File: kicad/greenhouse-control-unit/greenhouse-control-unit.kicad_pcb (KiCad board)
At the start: 2 copper layers, 252.1 x 133.3 mm, 43 parts, among them J1 Screw_Terminal_01x02, J10_Buck2 Conn_01x01_Female, J11_Buck2 Conn_01x01_Female, J12_Buck1 Conn_01x01_Female, J13_Buck1 Conn_01x01_Female, J14_Buck2 Conn_01x01_Female, J15_Buck2 Conn_01x01_Female, J16 Screw_Terminal_01x16, J2 Screw_Terminal_01x02, J3 Screw_Terminal_01x02, J4 Screw_Terminal_01x06, J5 Conn_01x03_Male, J6 Conn_01x02_Male, J6_BigBuck1 Conn_01x01_Female, J7_Buck1 Conn_01x01_Female, J8 Conn_01x15_Female, J9 Conn_01x15_Female, Q1 IRLB8721PBF, Q2 IRLB8721PBF, Q3 IRLB8721PBF, Q4 IRLB8721PBF, Q6 2N2222A, Q7 2N2222A, Q8 2N2222A, Q9 IRLB8721PBF, U1 74HC595, U2 74HC595

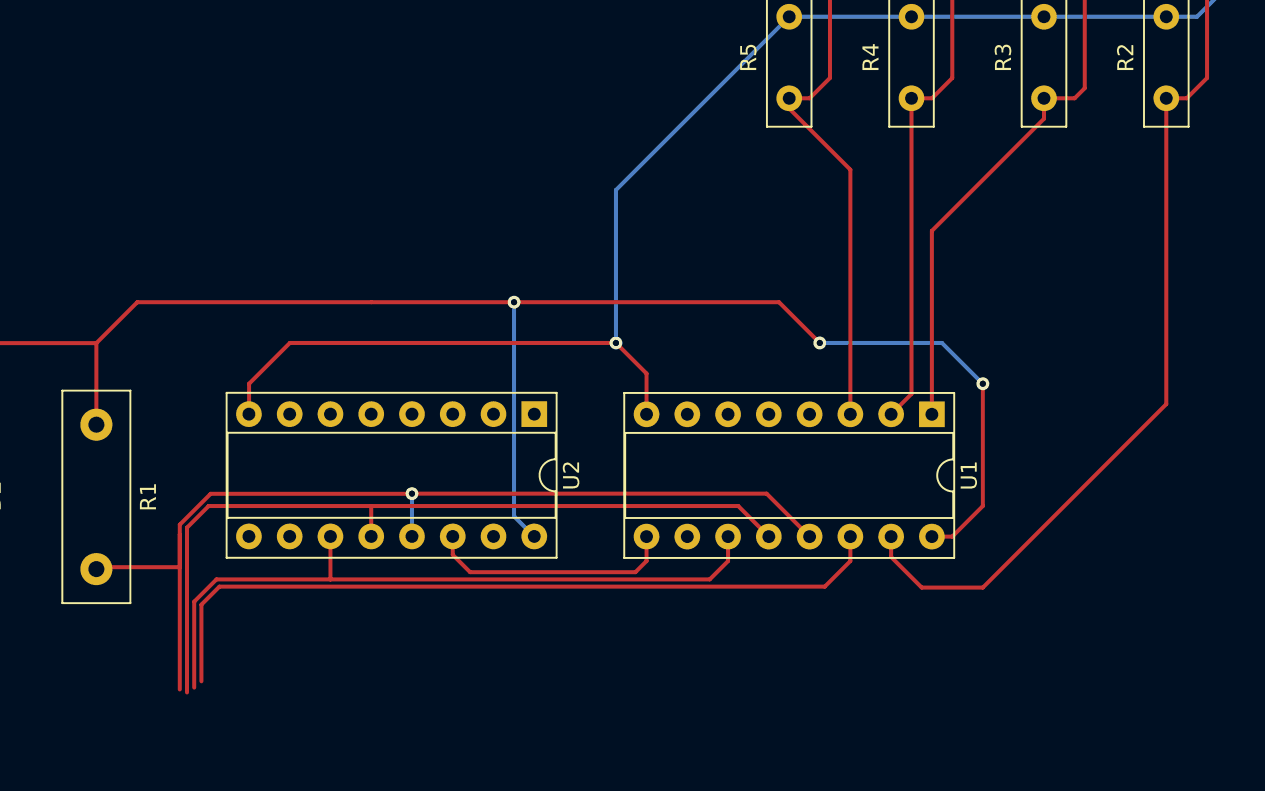
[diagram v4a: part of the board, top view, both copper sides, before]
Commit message: Swap U1 and U2 positions on PCB
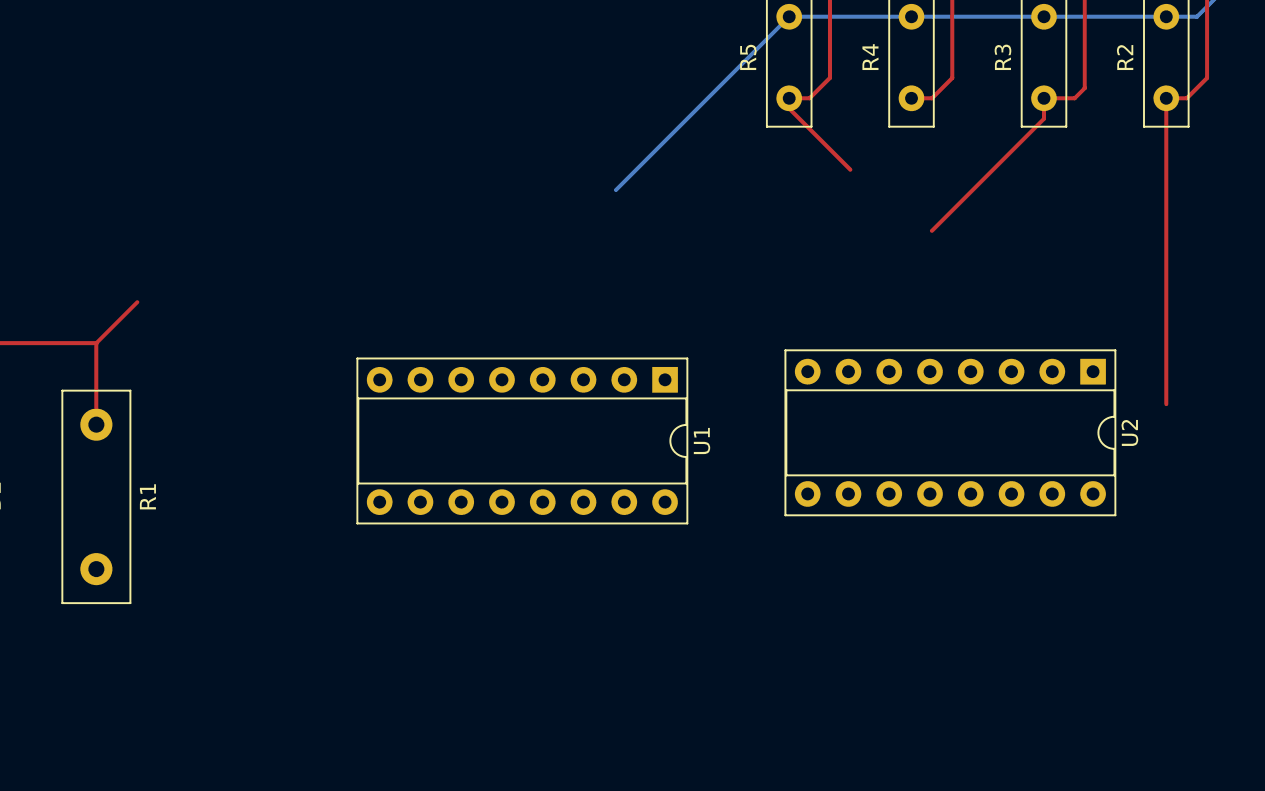
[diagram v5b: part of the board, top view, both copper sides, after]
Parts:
- moved U2 34.9 mm to (187.2, 80.5)
- moved U1 16.8 mm to (160.5, 81.0)
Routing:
- net /SR_VCC: track 102.4 -> 20.9 mm, vias 3 -> 0
- net /MC_D8: track 61.4 -> 0.17 mm, vias 1 -> 0
- net /MC_D5: track 106.3 -> 56.5 mm
- net /MC_D6: track 105.8 -> 57.9 mm
- net /MC_D7: track 103.2 -> 59.3 mm
- net GND: track 353.1 -> 311.9 mm, vias 4 -> 3
- net /SW1_SR_Q08: track 58.1 -> 34.1 mm
- net /SW3_SR_Q10: track 35.3 -> 15.1 mm
- net Net-(U1-Pad9): track 15.5 -> 0.00 mm
- net /SW4_SR_Q11: track 36.3 -> 21.1 mm
- net /SW2_SR_Q09: track 38.0 -> 26.6 mm

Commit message: Rearranged PCB layout, re-annotate power connectors
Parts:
- removed the D4 at (203.8, 112.4)
- removed D5: 1N4001, Diode_THT:D_DO-41_SOD81_P10.16mm_Horizontal
- added J6: Screw_Terminal_01x02, TerminalBlock_Phoenix:TerminalBlock_Phoenix_MKDS-1,5-2-5.08_1x02_P5.08mm_Horizontal, F.Cu at (186.5, 34.0)
- added J7: Screw_Terminal_01x02, TerminalBlock_Phoenix:TerminalBlock_Phoenix_MKDS-1,5-2-5.08_1x02_P5.08mm_Horizontal, F.Cu at (171.0, 34.0)
- added J8: Conn_01x03_Male, Connector_Molex:Molex_KK-254_AE-6410-03A_1x03_P2.54mm_Vertical, F.Cu at (259.0, 50.0)
- J4: value Screw_Terminal_01x06 -> Screw_Terminal_01x02; footprint TerminalBlock_Phoenix:TerminalBlock_Phoenix_MKDS-1,5-6-5.08_1x06_P5.08mm_Horizontal -> TerminalBlock_Phoenix:TerminalBlock_Phoenix_MKDS-1,5-2-5.08_1x02_P5.08mm_Horizontal
- J5: value Conn_01x03_Male -> Screw_Terminal_01x02; footprint Connector_Molex:Molex_KK-254_AE-6410-03A_1x03_P2.54mm_Vertical -> TerminalBlock_Phoenix:TerminalBlock_Phoenix_MKDS-1,5-2-5.08_1x02_P5.08mm_Horizontal
- moved J5 111.7 mm to (202.0, 34.0), turned to 180 degrees
- moved J4 91.3 mm to (217.5, 34.0), turned to 180 degrees
- moved Q3 89.2 mm to (192.7, 63.4)
- moved Q2 68.5 mm to (263.0, 62.0), turned to 180 degrees
- moved J3 47.6 mm to (233.0, 34.0), turned to 180 degrees
- moved J12 43.1 mm to (152.6, 34.1)
- moved Q5 43.1 mm to (125.6, 53.7)
- moved Q6 43.1 mm to (149.1, 53.7)
- moved Q7 43.1 mm to (141.4, 53.7)
- moved Q8 43.1 mm to (133.2, 53.7)
- moved R6 43.1 mm to (125.3, 65.2)
- moved R7 43.1 mm to (148.8, 65.2)
- moved R8 43.1 mm to (141.1, 65.2)
- moved R9 43.1 mm to (132.9, 65.2)
- moved BZ1 37.7 mm to (190.2, 144.0)
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- renumbered D2 to D1, D6 to D2, D1 to D4, J9 to J10, J10_Buck2 to J10_LittleBuck1, J6 to J11, J11_Buck2 to J11_LittleBuck1, J16 to J12, J12_Buck1 to J12_BigBuck1, J13_Buck1 to J13_BigBuck1, J14_Buck2 to J14_LittleBuck1, J15_Buck2 to J15_LittleBuck1, J7_Buck1 to J7_BigBuck1, J8 to J9, Q9 to Q1, Q8 to Q2, Q6 to Q3, Q7 to Q4, Q4 to Q5, Q1 to Q6, Q2 to Q7, Q3 to Q8, R6 to R2, R9 to R3, R8 to R4, R7 to R5, R5 to R6, R2 to R7, R3 to R8, R4 to R9
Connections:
- J1 pad 2: +12V -> /BattRelayNC_B
- J3 pad 1: GND -> /Batt+12V
- J3 pad 2: +12V -> /BattRelayNC_B
- J5 pad 1: +12V -> GND
- J5 pad 2: GND -> /BattRelayNC_B
- Q1 pad 2: /BattRelayNC_Coil -> /BattRelayNC_Boil
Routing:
- net +12V: track 490.2 -> 80.4 mm, vias 2 -> 0
- net /SR_VCC: track 20.9 -> 102.4 mm, vias 0 -> 3
- net /Batt+12V: track 69.8 -> 0.00 mm
- net /MC_D8: track 0.17 -> 61.4 mm, vias 0 -> 1
- net /MC_D5: track 56.5 -> 106.3 mm
- net /MC_D6: track 57.9 -> 105.8 mm
- net GND: track 311.9 -> 266.6 mm, vias 3 -> 2
- net /MC_D7: track 59.3 -> 103.2 mm
- net /BattRelayNC_SR_Q0: track 0.00 -> 23.9 mm
- net /SW1_SR_Q08: track 34.1 -> 15.1 mm
- net Net-(U1-Pad9): track 0.00 -> 15.5 mm
- net /SW2_SR_Q09: track 26.6 -> 16.7 mm
- net /SW4_SR_Q11: track 21.1 -> 15.7 mm
- net /CaseFan_SR_Q2: track 0.00 -> 1.80 mm
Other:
- board outline removed

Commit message: Add PSU diode, reorganize PCB layout
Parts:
- removed the J6 at (186.5, 34.0)
- added D1: D_Schottky, Package_TO_SOT_THT:TO-126-2_Vertical, F.Cu at (160.5, 34.4)
- added D2: LED, LED_THT:LED_D5.0mm, F.Cu at (162.0, 47.2)
- added D7: LED, LED_THT:LED_D5.0mm, F.Cu at (176.0, 47.0)
- added J13: Conn_01x10_Female, Connector_Molex:Molex_KK-254_AE-6410-10A_1x10_P2.54mm_Vertical, F.Cu at (47.0, 34.0)
- added J8: Conn_01x10_Female, Connector_PinSocket_2.54mm:PinSocket_1x10_P2.54mm_Vertical, F.Cu at (96.5, 97.0)
- added R1: 5k, Resistor_THT:R_Axial_DIN0207_L6.3mm_D2.5mm_P7.62mm_Horizontal, F.Cu at (176.0, 65.2)
- added R16: R10k, Resistor_THT:R_Axial_DIN0207_L6.3mm_D2.5mm_P7.62mm_Horizontal, F.Cu at (133.7, 57.2)
- added R2: 10k, Resistor_THT:R_Axial_DIN0207_L6.3mm_D2.5mm_P7.62mm_Horizontal, F.Cu at (183.0, 72.8)
- added R3: 5k, Resistor_THT:R_Axial_DIN0207_L6.3mm_D2.5mm_P7.62mm_Horizontal, F.Cu at (162.0, 65.2)
- added R4: 10k, Resistor_THT:R_Axial_DIN0207_L6.3mm_D2.5mm_P7.62mm_Horizontal, F.Cu at (169.0, 72.8)
- added R5: 10k, Resistor_THT:R_Axial_DIN0207_L6.3mm_D2.5mm_P7.62mm_Horizontal, F.Cu at (162.0, 60.8)
- added R6: 10k, Resistor_THT:R_Axial_DIN0207_L6.3mm_D2.5mm_P7.62mm_Horizontal, F.Cu at (102.5, 87.0)
- J10, J9: footprint Connector_PinHeader_2.54mm:PinHeader_1x15_P2.54mm_Vertical -> Connector_PinSocket_2.54mm:PinSocket_1x15_P2.54mm_Vertical
- J12_BigBuck1, J13_BigBuck1, J6_BigBuck1, J7_BigBuck1: footprint Connector_PinHeader_2.54mm:PinHeader_1x01_P2.54mm_Vertical -> Connector_PinSocket_2.54mm:PinSocket_1x01_P2.54mm_Vertical
- J7: value Screw_Terminal_01x02 -> Conn_01x10_Female; footprint TerminalBlock_Phoenix:TerminalBlock_Phoenix_MKDS-1,5-2-5.08_1x02_P5.08mm_Horizontal -> Connector_PinSocket_2.54mm:PinSocket_1x10_P2.54mm_Vertical
- R10: renamed from R2; value 10k -> R4k6; footprint Resistor_THT:R_Box_L8.4mm_W2.5mm_P5.08mm -> Resistor_THT:R_Axial_DIN0207_L6.3mm_D2.5mm_P7.62mm_Horizontal
- R11: renamed from R3; value 10k -> 2k; footprint Resistor_THT:R_Box_L8.4mm_W2.5mm_P5.08mm -> Resistor_THT:R_Axial_DIN0207_L6.3mm_D2.5mm_P7.62mm_Horizontal
- R12: renamed from R6; value R10k -> 2k; footprint Resistor_THT:R_Box_L8.4mm_W2.5mm_P5.08mm -> Resistor_THT:R_Axial_DIN0207_L6.3mm_D2.5mm_P7.62mm_Horizontal
- R13: renamed from R7; footprint Resistor_THT:R_Box_L8.4mm_W2.5mm_P5.08mm -> Resistor_THT:R_Axial_DIN0207_L6.3mm_D2.5mm_P7.62mm_Horizontal
- R14: renamed from R8; footprint Resistor_THT:R_Box_L8.4mm_W2.5mm_P5.08mm -> Resistor_THT:R_Axial_DIN0207_L6.3mm_D2.5mm_P7.62mm_Horizontal
- R15: renamed from R9; footprint Resistor_THT:R_Box_L8.4mm_W2.5mm_P5.08mm -> Resistor_THT:R_Axial_DIN0207_L6.3mm_D2.5mm_P7.62mm_Horizontal
- R7: renamed from R1; footprint Resistor_THT:R_Box_L13.0mm_W4.0mm_P9.00mm -> Resistor_THT:R_Axial_DIN0207_L6.3mm_D2.5mm_P7.62mm_Horizontal
- R8: renamed from R4; value R10k -> 2k; footprint Resistor_THT:R_Box_L8.4mm_W2.5mm_P5.08mm -> Resistor_THT:R_Axial_DIN0207_L6.3mm_D2.5mm_P7.62mm_Horizontal
- R9: renamed from R5; value R4k6 -> R10k; footprint Resistor_THT:R_Box_L13.0mm_W4.0mm_P9.00mm -> Resistor_THT:R_Axial_DIN0207_L6.3mm_D2.5mm_P7.62mm_Horizontal
- moved Q4 162.0 mm to (79.2, 43.4)
- moved J11 161.5 mm to (79.2, 34.0)
- moved Q1 119.8 mm to (207.0, 48.0), turned to 180 degrees
- moved D5 118.0 mm to (230.2, 120.0)
- moved J7 112.3 mm to (78.0, 96.9)
- moved R10 110.1 mm to (239.2, 124.0)
- moved R8 105.0 mm to (218.0, 60.5), turned to 90 degrees
- moved R11 95.8 mm to (190.0, 60.8), turned to 90 degrees
- moved D4 95.1 mm to (218.0, 47.0), turned to -90 degrees
- moved D6 94.3 mm to (190.0, 47.0), turned to -90 degrees
- moved J1 85.5 mm to (178.5, 34.0)
- moved J9 81.9 mm to (35.0, 64.4), turned to 0 degrees
- moved J14_LittleBuck1 69.2 mm to (217.0, 86.8)
- moved J15_LittleBuck1 69.2 mm to (232.9, 86.8)
- moved J10_LittleBuck1 69.2 mm to (217.0, 78.5)
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- renumbered D1 to D3, D2 to D5, D3 to D6, J8 to J6
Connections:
- net /MC_D6 renamed /SR_SER
- net /MC_D7 renamed /SR_CLK
- D4 pad 1: Net-(D4-Pad1) -> GND
- D4 pad 2: Net-(BZ1-Pad1) -> Net-(D4-Pad2)
- D5 pad 1: GND -> Net-(D5-Pad1)
- D5 pad 2: Net-(D2-Pad2) -> Net-(BZ1-Pad1)
- J1 pad 1: GND -> /PSU+12V
- J1 pad 2: /BattRelayNC_B -> GND
- J10 pad 1: /MC_D8 -> +3V3
- J10 pad 12: /MC_D3 -> /OneWire
- J10 pad 13: /I2C_SDA -> /ADC1_SCA
- J10 pad 14: /I2C_SCL -> /ADC1_SCL
- J10 pad 15: unconnected-(J10-Pad15) -> /MC_D0
- J2 pad 1: GND -> /Batt+12V
- J2 pad 2: /Batt+12V -> GND
- J3 pad 1: /Batt+12V -> +12V
- J3 pad 2: /BattRelayNC_B -> /Batt+12V
- J4 pad 1: GND -> /BattRelayNC_Coil
- J4 pad 2: /BattRelayNC_Coil -> GND
- J5 pad 1: GND -> +12V
- J5 pad 2: /BattRelayNC_B -> GND
- J7 pad 1: GND -> +5VA
- J7 pad 2: +12V -> GND
- J9 pad 1: /MC_A0 -> +5VA
- J9 pad 14: GND -> unconnected-(J9-Pad14)
- J9 pad 15: +5VA -> /MC_A0
- J9 pad 2: unconnected-(J9-Pad2) -> GND
- Q1 pad 2: /BattRelayNC_Boil -> /BattRelayNC_Coil
- R10 pad 1: /BatteryLed_SR_Q4 -> Net-(D5-Pad1)
- R10 pad 2: Net-(D2-Pad2) -> GND
- R11 pad 1: /PsuLed_SR_Q5 -> /BatteryLed_SR_Q4
- R12 pad 1: /SW4_SR_Q11 -> /PsuLed_SR_Q5
- R12 pad 2: GND -> Net-(D7-Pad2)
- R13 pad 1: /SW1_SR_Q08 -> /SW4_SR_Q11
- R14 pad 1: /SW2_SR_Q09 -> /SW1_SR_Q08
- R15 pad 1: /SW3_SR_Q10 -> /SW2_SR_Q09
- R7 pad 2: /MC_D8 -> /MC_D0
- R8 pad 1: GND -> /BattRelayNC_SR_Q0
- R8 pad 2: /StartBeep_SR_Q1 -> Net-(D4-Pad2)
- R9 pad 1: Net-(D4-Pad1) -> GND
- R9 pad 2: GND -> /StartBeep_SR_Q1
- U1 pad 13: /MC_D8 -> /MC_D0
- U2 pad 13: /MC_D8 -> /MC_D0
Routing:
- net +12V: track 80.4 -> 179.8 mm, vias 0 -> 1
- net GND: track 266.6 -> 335.8 mm
- net /MC_D0: track 0.00 -> 61.4 mm, vias 0 -> 1
- net /MC_D8: track 61.4 -> 0.00 mm, vias 1 -> 0
- net unconnected-(J10-Pad5): track 60.8 -> 0.00 mm
- net /SR_CLK: track 103.2 -> 43.9 mm
- net /SR_SER: track 105.8 -> 47.9 mm
- net /MC_D5: track 106.3 -> 49.8 mm
- net /PSU+12V: track 0.00 -> 52.5 mm, vias 0 -> 1
- net /BattRelayNC_Coil: track 0.00 -> 26.6 mm
- net /SW3_SR_Q10: track 15.1 -> 0.00 mm
- net /Batt+12V: track 0.00 -> 8.78 mm
- net /PSU_VoltageSensor_A: track 0.00 -> 7.00 mm
- net /COM_VoltageSensor_A: track 0.00 -> 7.00 mm
- net Net-(D7-Pad2): track 0.00 -> 3.65 mm
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
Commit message: Connect relay coil to VCC, fixed footprints
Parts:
- J5: value Screw_Terminal_01x02 -> Conn_01x02_Male; footprint TerminalBlock_Phoenix:TerminalBlock_Phoenix_MKDS-1,5-2-5.08_1x02_P5.08mm_Horizontal -> Connector_Molex:Molex_KK-254_AE-6410-02A_1x02_P2.54mm_Vertical
- moved J5 139.5 mm to (94.5, 39.0), turned to 0 degrees
- moved J6 128.3 mm to (115.9, 39.3)
- moved Q2 128.3 mm to (117.2, 51.2)
- moved R13 38.5 mm to (163.8, 71.0)
- moved D1 38.5 mm to (198.5, 40.6)
- moved D2 38.5 mm to (200.0, 53.4)
- moved D6 38.5 mm to (228.0, 53.2)
- moved D7 38.5 mm to (214.0, 53.2)
- moved J1 38.5 mm to (216.5, 40.2)
- moved J12 38.5 mm to (190.6, 40.3)
- moved J2 38.5 mm to (230.4, 40.2)
- moved J3 38.5 mm to (244.3, 40.2)
- moved J4 38.5 mm to (258.1, 40.2)
- moved Q1 38.5 mm to (245.0, 54.2)
- moved Q5 38.5 mm to (163.6, 59.9)
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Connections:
- net /COM_VoltageSensor_A renamed /ADC2_A0
- net /OneWire renamed /MC_D3
- net /PSU_VoltageSensor_A renamed /ADC2_A1
- net /SR_CLK renamed /MC_D7
- net /SR_SER renamed /MC_D6
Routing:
- net +12V: track 179.8 -> 147.0 mm
- net GND: track 335.8 -> 321.8 mm
